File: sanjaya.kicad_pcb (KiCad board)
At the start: 2 copper layers, 101 x 47 mm, 94 parts, among them J1 PWR_SUPPLY, J10 Bat_Bak_Byp_Gnd, J11 Board_PwrIn, J12 ON_Switch, J13 Raspberry_Pi_2_3, J14 Fan, J15 RS232, J16 RS485, J17 I2C, J18 Bat_Bak_Byp_Vcc, J2 Digital_Input_Signals, J3 Digital_Input_Gnd, J4 Screw_Terminal_01x03, J5 Screw_Terminal_01x03, J6 Analog_RSense, J7 Analog_420, J8 Supply_Safety_Bypass, J9 To_PwrBank, K1 Songle-SRD, K2 Songle-SRD, Q1 Q_PMOS_GSD, Q2 FDC021N30, SW2 SW_DIP_x04, U1 74HC14, U2 MCP9700T-ETT, U3 TPS2400BVR, U4 ULN2803A, U5 MCP3428, U6 TLP291-4, U7 MAX232, U8 SN65HVD75DR

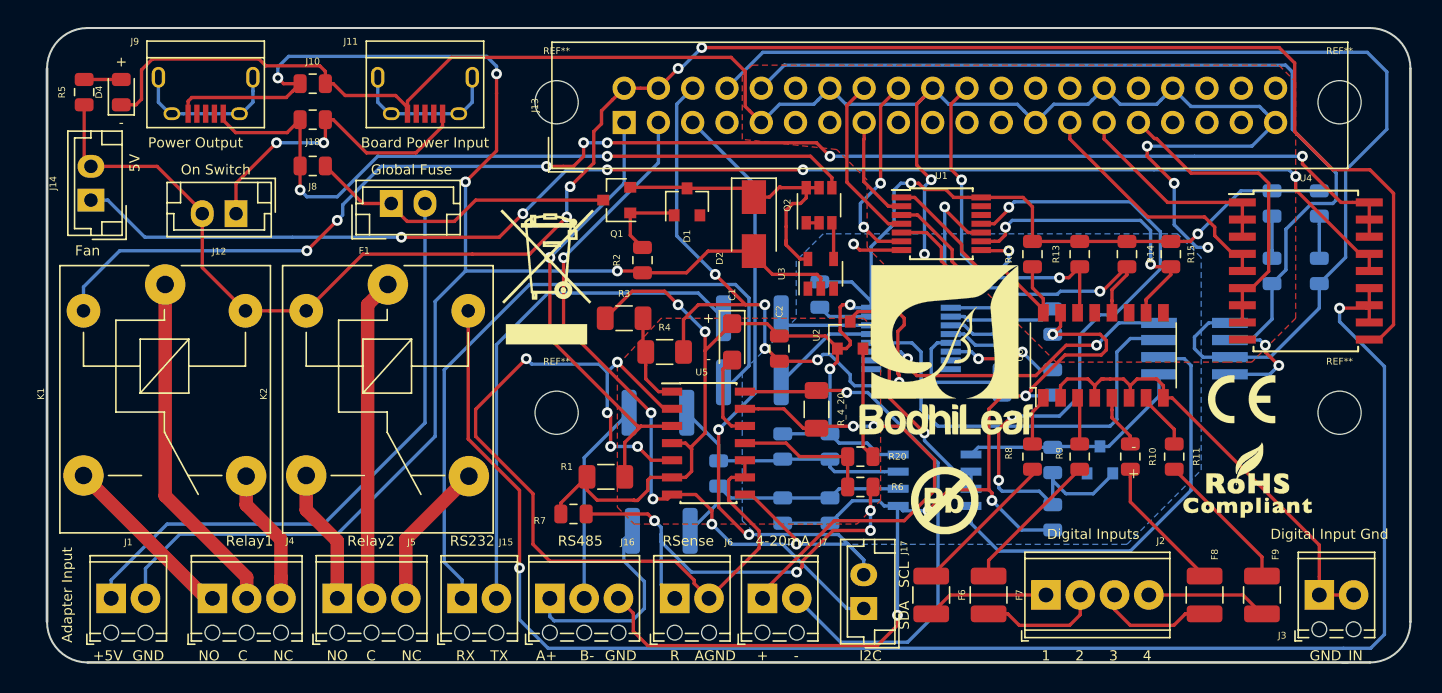
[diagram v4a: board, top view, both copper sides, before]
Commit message: Changes: 1. Corrected RS485 circuit connections 2. Added silk screen labels and labels to schematics
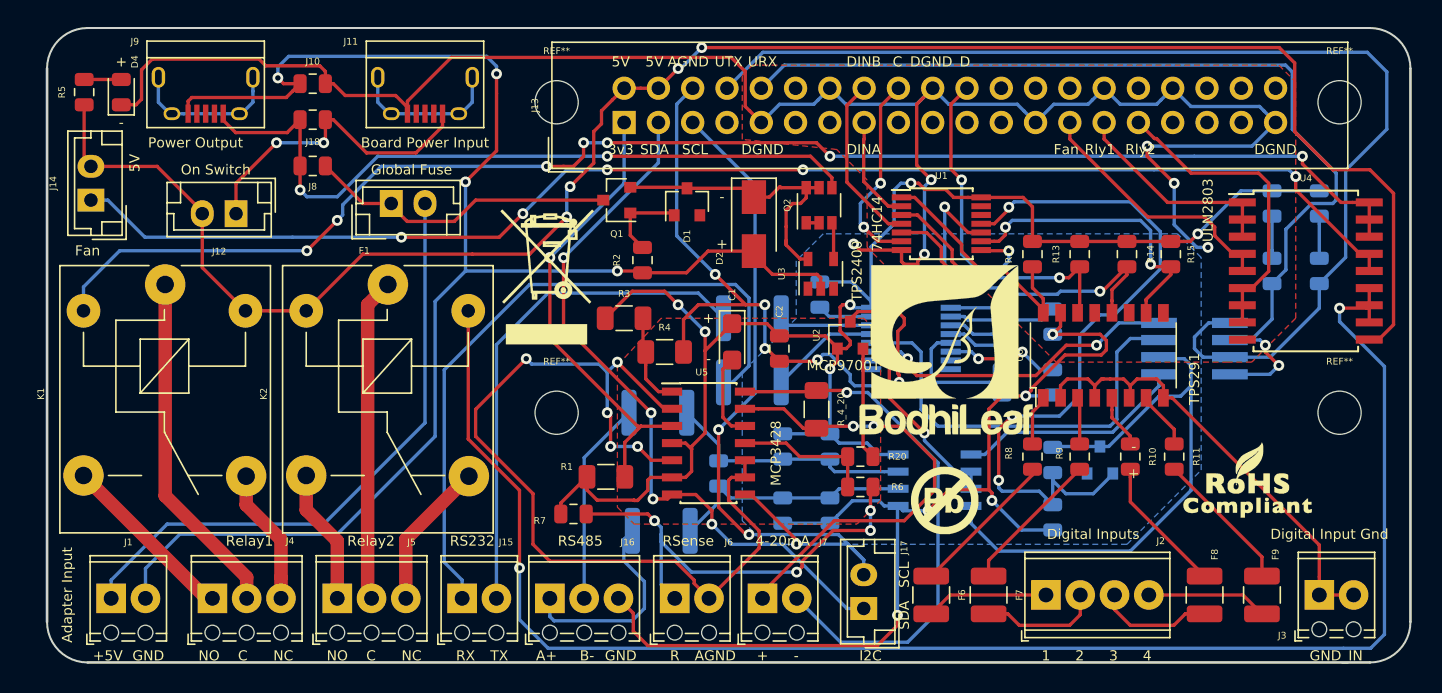
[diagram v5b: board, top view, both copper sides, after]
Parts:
- removed the G*** at (162.5, 110.0)
- removed the G*** at (116.5, 98.0)
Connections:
- J11 pad 2: Net-(J11-Pad2) -> (no net)
- J11 pad 3: Net-(J11-Pad3) -> (no net)
- J11 pad 4: Net-(J11-Pad4) -> (no net)
- J13 pad 11: Net-(J13-Pad11) -> (no net)
- J13 pad 12: Net-(J13-Pad12) -> (no net)
- J13 pad 13: Net-(J13-Pad13) -> (no net)
- J13 pad 17: Net-(J13-Pad17) -> (no net)
- J13 pad 19: Net-(J13-Pad19) -> (no net)
- J13 pad 21: Net-(J13-Pad21) -> (no net)
- J13 pad 23: Net-(J13-Pad23) -> (no net)
- J13 pad 24: Net-(J13-Pad24) -> (no net)
- J13 pad 26: Net-(J13-Pad26) -> (no net)
- J13 pad 28: Net-(J13-Pad28) -> (no net)
- J13 pad 32: Net-(J13-Pad32) -> (no net)
- J13 pad 33: Net-(J13-Pad33) -> (no net)
- J13 pad 35: Net-(J13-Pad35) -> (no net)
- J13 pad 36: Net-(J13-Pad36) -> (no net)
- J13 pad 37: Net-(J13-Pad37) -> (no net)
- J13 pad 38: Net-(J13-Pad38) -> (no net)
- J13 pad 40: Net-(J13-Pad40) -> (no net)
- J13 pad 7: Net-(J13-Pad7) -> (no net)
- J9 pad 2: Net-(J9-Pad2) -> (no net)
- J9 pad 3: Net-(J9-Pad3) -> (no net)
- J9 pad 4: Net-(J9-Pad4) -> (no net)
- SW2 pad 5: Net-(D3-Pad1) -> Net-(SW2-Pad5)
- SW2 pad 6: Net-(SW2-Pad6) -> Net-(D3-Pad1)
- U3 pad 1: Net-(U3-Pad1) -> (no net)
- U3 pad 3: Net-(U3-Pad3) -> (no net)
- U7 pad 10: Net-(U7-Pad10) -> (no net)
- U7 pad 7: Net-(U7-Pad7) -> (no net)
- U7 pad 8: Net-(U7-Pad8) -> (no net)
- U7 pad 9: Net-(U7-Pad9) -> (no net)
- U8 pad 1: Net-(D3-Pad1) -> Net-(SW2-Pad5)
- U8 pad 4: Net-(SW2-Pad6) -> Net-(D3-Pad1)
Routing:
- net Net-(SW2-Pad6): track 32.2 -> 0.00 mm
- net Net-(D3-Pad1): track 17.3 -> 44.3 mm
- net Net-(SW2-Pad5): track 0.00 -> 16.9 mm
- net /DGND: track 224.8 -> 227.9 mm
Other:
- board text added: "3v3"
- board text added: "74HC14"
- board text added: "D"
- board text added: "DGND"
- board text added: "DINA"
- board text added: "DINB"
- board text added: "MCP3428"
- board text added: "MCP9700T"
- board text added: "Rly1"
- board text added: "Rly2"
- board text added: "TPS2400"
- board text added: "TPS291"
- board text added: "ULN2803"
- board text added: "URX"
- board text added: "UTX"
